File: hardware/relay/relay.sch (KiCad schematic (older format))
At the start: 18 parts, among them J1 GS3, J2 GS3, J3 CONN_02X04, J4 CONN_01X04, Q1 BC817-40, Q2 BC817-40, U1 ATTINY85-20SU, U2 ATTINY85-20PU

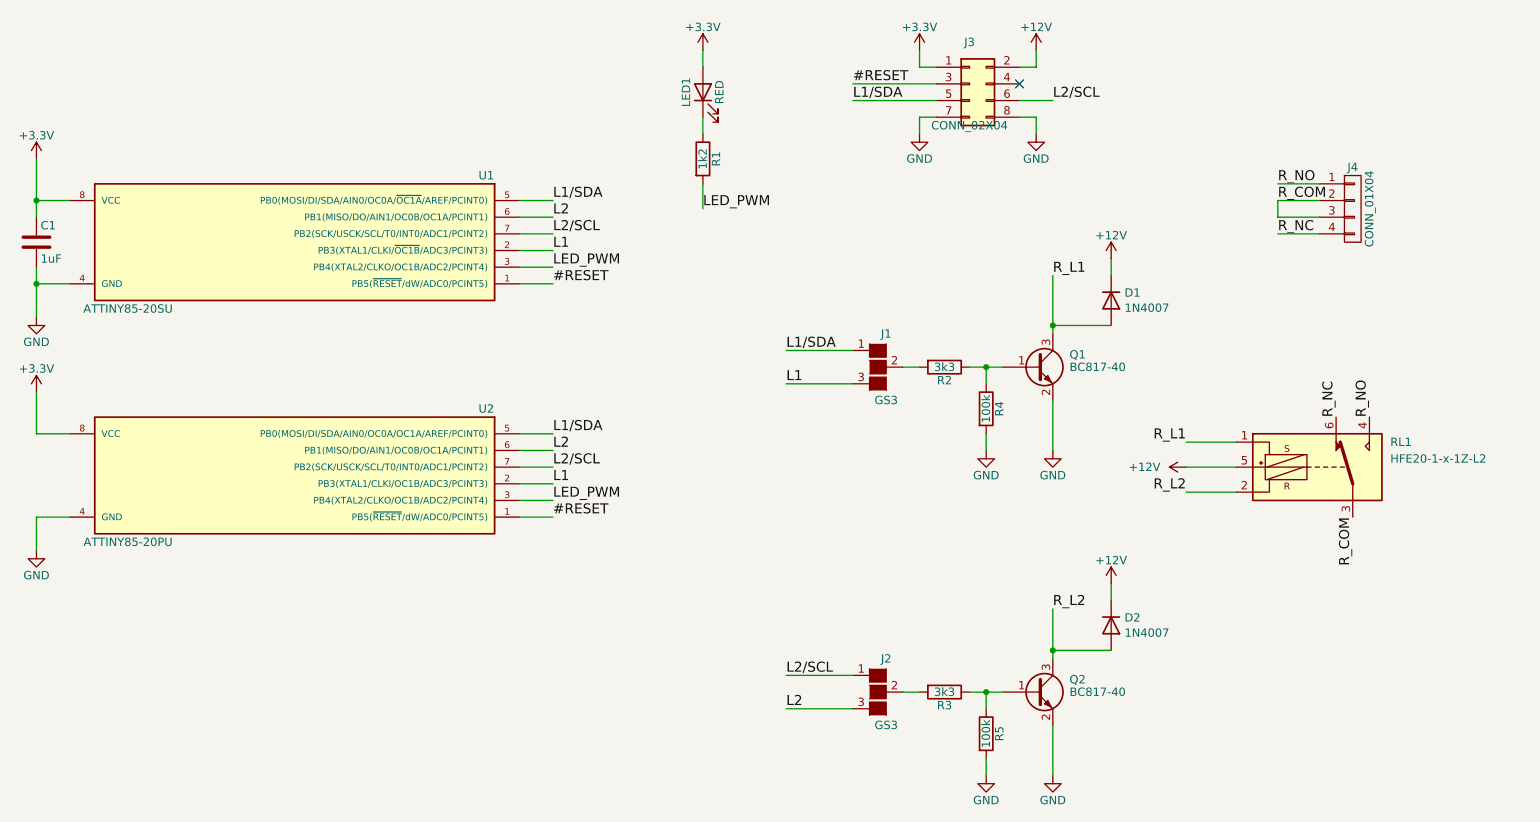
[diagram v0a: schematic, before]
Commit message: Add power flag, convert label to global labels, add R to protect #RESET
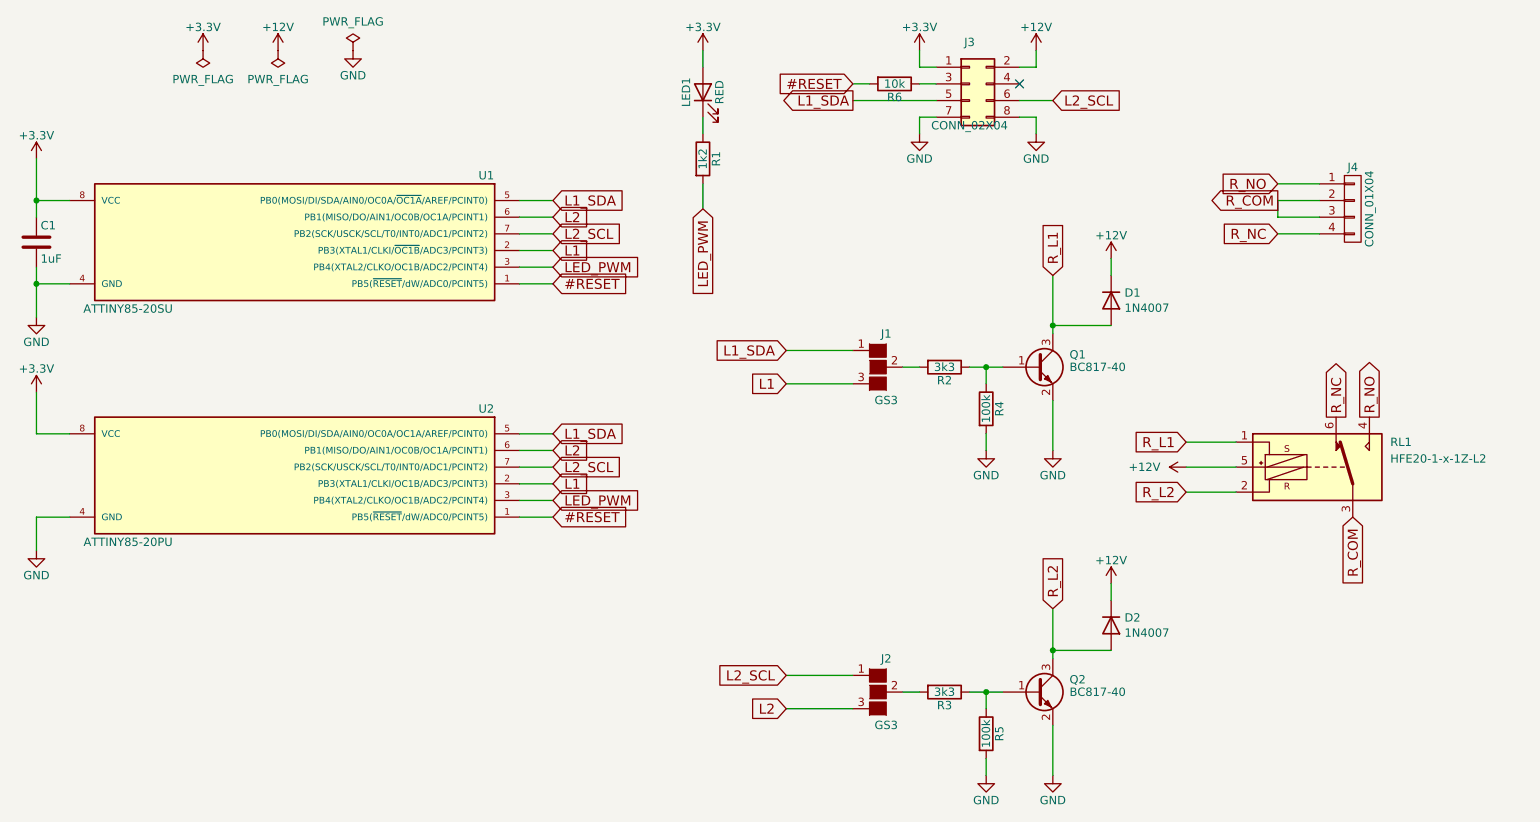
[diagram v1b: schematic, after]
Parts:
- added R6: 10k, Resistors_SMD:R_0805_HandSoldering, symbol Device:R
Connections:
- net #RESET: now also R6.2; no longer J3.3 (Pin_3)
- net L1/SDA renamed L1_SDA
- net L2/SCL renamed L2_SCL
- new net: J3.3 (Pin_3), R6.1
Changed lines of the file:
@@
 Wire Wire Line
 	7800 5150 7800 5250
-Text Label 6600 2900 0    60   ~ 0
-L1
-Text Label 6600 2700 0    60   ~ 0
-L1/SDA
 Wire Wire Line
 	6600 2700 7000 2700
 Wire Wire Line
 	6600 2900 7000 2900
-Text Label 6600 4650 0    60   ~ 0
-L2/SCL
-Text Label 6600 4850 0    60   ~ 0
-L2
 Wire Wire Line
 	6600 4850 7000 4850
 Wire Wire Line
 	6600 4650 7000 4650
-Text Label 8200 4250 0    60   ~ 0
-R_L2
-Text Label 8200 2250 0    60   ~ 0
-R_L1
 $Comp
 L power:+3.3V #PWR09
@@
 Wire Wire Line
 	2100 3700 2100 3900
-Text Label 5200 2300 0    60   ~ 0
-#RESET
-Text Label 5200 2200 0    60   ~ 0
-LED_PWM
-Text Label 5200 2100 0    60   ~ 0
-L1
-Text Label 5200 2000 0    60   ~ 0
-L2/SCL
-Text Label 5200 1900 0    60   ~ 0
-L2
-Text Label 5200 1800 0    60   ~ 0
-L1/SDA
 Wire Wire Line
 	5000 1800 5200 1800
@@
 Connection ~ 2100 1800
 Connection ~ 2100 2300
-Text Label 6100 1850 0    60   ~ 0
-LED_PWM
 $Comp
 L power:GND #PWR013
@@
 Wire Wire Line
 	7400 1300 7400 1400
-Text Label 7000 1200 0    60   ~ 0
-L1/SDA
-Text Label 8200 1200 0    60   ~ 0
-L2/SCL
-Text Label 7000 1100 0    60   ~ 0
-#RESET
-Wire Wire Line
-	7000 1100 7500 1100
+Wire Wire Line
+	7000 1100 7100 1100
 Wire Wire Line
 	7000 1200 7500 1200
 Wire Wire Line
 	8000 1200 8200 1200
-Text Label 5200 3700 0    60   ~ 0
-#RESET
-Text Label 5200 3600 0    60   ~ 0
-LED_PWM
-Text Label 5200 3500 0    60   ~ 0
-L1
-Text Label 5200 3400 0    60   ~ 0
-L2/SCL
-Text Label 5200 3300 0    60   ~ 0
-L2
-Text Label 5200 3200 0    60   ~ 0
-L1/SDA
 Wire Wire Line
 	5000 3200 5200 3200
@@
 Wire Wire Line
 	9800 2000 9550 2000
-Text Label 9550 1700 0    60   ~ 0
-R_NO
-Text Label 9550 1800 0    60   ~ 0
-R_COM
-Text Label 9550 2000 0    60   ~ 0
-R_NC
 $Comp
 L power:+12V #PWR014
@@
 Wire Wire Line
 	9300 3400 9000 3400
-Text Label 9000 3250 2    60   ~ 0
-R_L1
-Text Label 9000 3550 2    60   ~ 0
-R_L2
-Text Label 10100 3100 1    60   ~ 0
-R_NO
-Text Label 10000 3700 3    60   ~ 0
-R_COM
 $Comp
 L 000-local-symbol:HFE20-1-x-1Z-x-x-L2 RL1
@@
 	1    0    0    -1
 $EndComp
-Text Label 9900 3100 1    60   ~ 0
-R_NC
 Wire Wire Line
 	7800 2800 7900 2800
@@
 	1    0    0    -1
 $EndComp
+Text GLabel 5200 1800 2    60   Input ~ 0
+L1_SDA
+Text GLabel 7000 1200 0    60   Output ~ 0
+L1_SDA
+Text GLabel 7000 1100 0    60   Input ~ 0
+#RESET
+Text GLabel 8200 1200 2    60   Input ~ 0
+L2_SCL
+Text GLabel 6600 2700 0    60   Input ~ 0
+L1_SDA
+Text GLabel 6600 2900 0    60   Input ~ 0
+L1
+Text GLabel 5200 3200 2    60   Input ~ 0
+L1_SDA
+Text GLabel 5200 3300 2    60   Input ~ 0
+L2
+Text GLabel 5200 3400 2    60   Input ~ 0
+L2_SCL
+Text GLabel 5200 3500 2    60   Input ~ 0
+L1
+Text GLabel 5200 3600 2    60   Input ~ 0
+LED_PWM
+Text GLabel 5200 3700 2    60   Input ~ 0
+#RESET
+Text GLabel 5200 1900 2    60   Input ~ 0
+L2
+Text GLabel 5200 2000 2    60   Input ~ 0
+L2_SCL
+Text GLabel 5200 2100 2    60   Input ~ 0
+L1
+Text GLabel 5200 2200 2    60   Input ~ 0
+LED_PWM
+Text GLabel 5200 2300 2    60   Input ~ 0
+#RESET
+Text GLabel 6100 1850 3    60   Input ~ 0
+LED_PWM
+Text GLabel 9000 3250 0    60   Input ~ 0
+R_L1
+Text GLabel 9000 3550 0    60   Input ~ 0
+R_L2
+Text GLabel 6600 4650 0    60   Input ~ 0
+L2_SCL
+Text GLabel 6600 4850 0    60   Input ~ 0
+L2
+Text GLabel 8200 4250 1    60   Input ~ 0
+R_L2
+Text GLabel 8200 2250 1    60   Input ~ 0
+R_L1
+Text GLabel 9550 1700 0    60   Input ~ 0
+R_NO
+Text GLabel 9550 1800 0    60   Output ~ 0
+R_COM
+Text GLabel 9550 2000 0    60   Input ~ 0
+R_NC
+Text GLabel 9900 3100 1    60   Output ~ 0
+R_NC
+Text GLabel 10100 3100 1    60   Output ~ 0
+R_NO
+Text GLabel 10000 3700 3    60   Input ~ 0
+R_COM
+$Comp
+L Device:R R6
+U 1 1 60199072
+P 7250 1100
+F 0 "R6" V 7330 1100 50  0000 C CNN
+F 1 "10k" V 7250 1100 50  0000 C CNN
+F 2 "Resistors_SMD:R_0805_HandSoldering" V 7180 1100 50  0001 C CNN
+F 3 "" H 7250 1100 50  0001 C CNN
+	1    7250 1100
+	0    1    1    0
+$EndComp
+Wire Wire Line
+	7400 1100 7500 1100
+$Comp
+L power:PWR_FLAG #FLG0101
+U 1 1 601B2756
+P 3100 900
+F 0 "#FLG0101" H 3100 975 50  0001 C CNN
+F 1 "PWR_FLAG" H 3100 1073 50  0000 C CNN
+F 2 "" H 3100 900 50  0001 C CNN
+F 3 "~" H 3100 900 50  0001 C CNN
+	1    3100 900
+	-1   0    0    1
+$EndComp
+$Comp
+L power:PWR_FLAG #FLG0102
+U 1 1 601B3140
+P 3550 900
+F 0 "#FLG0102" H 3550 975 50  0001 C CNN
+F 1 "PWR_FLAG" H 3550 1073 50  0000 C CNN
+F 2 "" H 3550 900 50  0001 C CNN
+F 3 "~" H 3550 900 50  0001 C CNN
+	1    3550 900
+	-1   0    0    1
+$EndComp
+$Comp
+L power:PWR_FLAG #FLG0103
+U 1 1 601B3635
+P 4000 900
+F 0 "#FLG0103" H 4000 975 50  0001 C CNN
+F 1 "PWR_FLAG" H 4000 1073 50  0000 C CNN
+F 2 "" H 4000 900 50  0001 C CNN
+F 3 "~" H 4000 900 50  0001 C CNN
+	1    4000 900
+	1    0    0    -1
+$EndComp
+$Comp
+L power:+3.3V #PWR0104
+U 1 1 601B3B42
+P 3100 900
+F 0 "#PWR0104" H 3100 750 50  0001 C CNN
+F 1 "+3.3V" H 3100 1040 50  0000 C CNN
+F 2 "" H 3100 900 50  0001 C CNN
+F 3 "" H 3100 900 50  0001 C CNN
+	1    3100 900
+	1    0    0    -1
+$EndComp
+$Comp
+L power:+12V #PWR0105
+U 1 1 601B3FB2
+P 3550 900
+F 0 "#PWR0105" H 3550 750 50  0001 C CNN
+F 1 "+12V" H 3550 1040 50  0000 C CNN
+F 2 "" H 3550 900 50  0001 C CNN
+F 3 "" H 3550 900 50  0001 C CNN
+	1    3550 900
+	1    0    0    -1
+$EndComp
+$Comp
+L power:GND #PWR0106
+U 1 1 601B45F6
+P 4000 900
+F 0 "#PWR0106" H 4000 650 50  0001 C CNN
+F 1 "GND" H 4000 750 50  0000 C CNN
+F 2 "" H 4000 900 50  0001 C CNN
+F 3 "" H 4000 900 50  0001 C CNN
+	1    4000 900
+	1    0    0    -1
+$EndComp
